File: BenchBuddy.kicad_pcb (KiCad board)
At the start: 4 copper layers, 165.1 x 63.5 mm, 56 parts, among them K1 1461069-5, P1 24 pin MiniFit JR, P2 CONN_3X2, P3 CONN_2, P4 12 pin Terminal Block, P5 3 Pin TB, Q1 2N3904, U1 MCP3901, U2 OPA4170, U3 LMT84, U9 LTV-816S

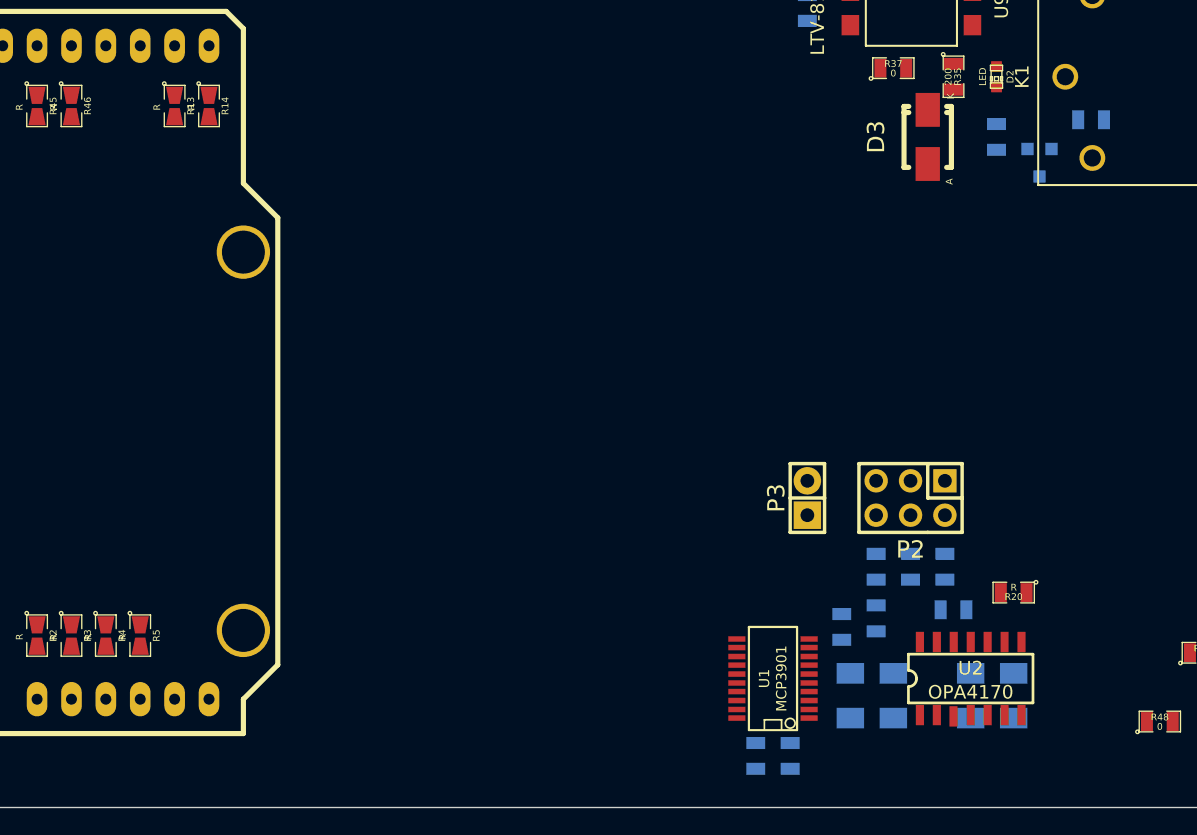
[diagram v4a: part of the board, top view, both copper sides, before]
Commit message: Associating and Placing the Current/Fan Driver Module
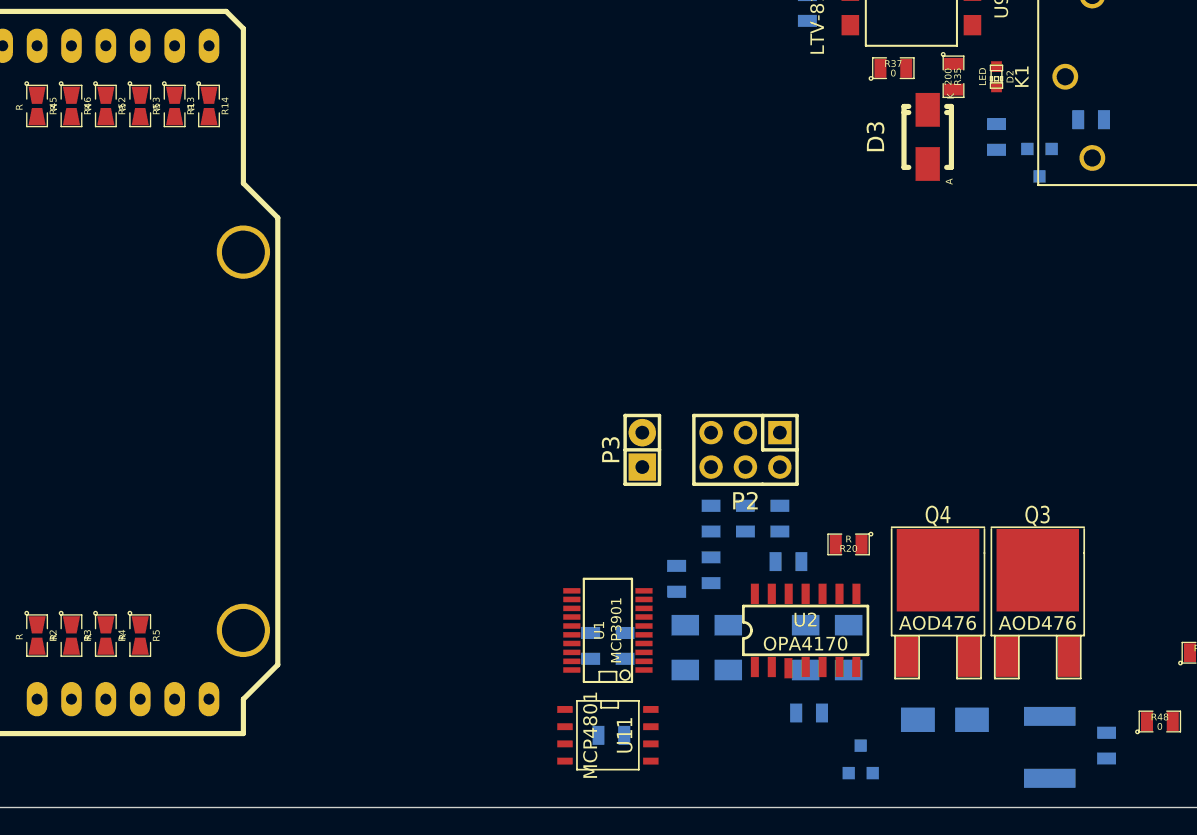
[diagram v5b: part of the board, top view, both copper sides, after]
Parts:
- added C10: C, SMD_Packages:SM0805, B.Cu at (165.9, 114.0)
- added C11: C, SMD_Packages:SM0805, B.Cu at (202.4, 114.8)
- added D5: B130-13-F, Diodes_SMD:Diode-SMA_Standard, B.Cu at (190.5, 112.9)
- added Q2: DMN65D8L-7, SMD_Packages:SOT23GDS, B.Cu at (184.3, 115.8)
- added Q3: AOD476, SMD_Packages:DPAKGDS, F.Cu at (197.4, 108.2)
- added Q4: AOD476, SMD_Packages:DPAKGDS, F.Cu at (190.0, 108.2)
- added R41: R, SMD_Packages:SM0805, B.Cu at (180.5, 112.4)
- added R42: R, SMD_Packages:SM1206, B.Cu at (193.5, 101.6)
- added R52: R, BenchBudEE:SM0805-Bridge, F.Cu at (128.5, 67.6)
- added R53: R, BenchBudEE:SM0805-Bridge, F.Cu at (131.1, 67.6)
- added TH5: PTC, SMD_Packages:SM1812, B.Cu at (198.2, 114.9)
- added U11: MCP4801, SMD_Packages:SO8N, F.Cu at (165.6, 114.0)
- moved C6 14.7 mm to (164.3, 107.4)
- moved C7 14.7 mm to (166.9, 107.4)
- moved C1 12.7 mm to (170.7, 102.5)
- moved P2 12.7 mm to (175.8, 93.0)
- moved P3 12.7 mm to (168.1, 93.0)
- moved R17 12.7 mm to (174.5, 107.6)
- moved R18 12.7 mm to (183.4, 107.6)
- moved R19 12.7 mm to (180.2, 107.6)
- moved R20 12.7 mm to (183.4, 99.9)
- moved R21 12.7 mm to (178.3, 98.0)
- moved R44 12.7 mm to (175.8, 98.0)
- moved U1 12.7 mm to (165.6, 106.3)
- moved U2 12.7 mm to (180.2, 106.3)
- moved C8 12.7 mm to (178.9, 101.2)
- moved R16 12.7 mm to (171.3, 107.6)
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
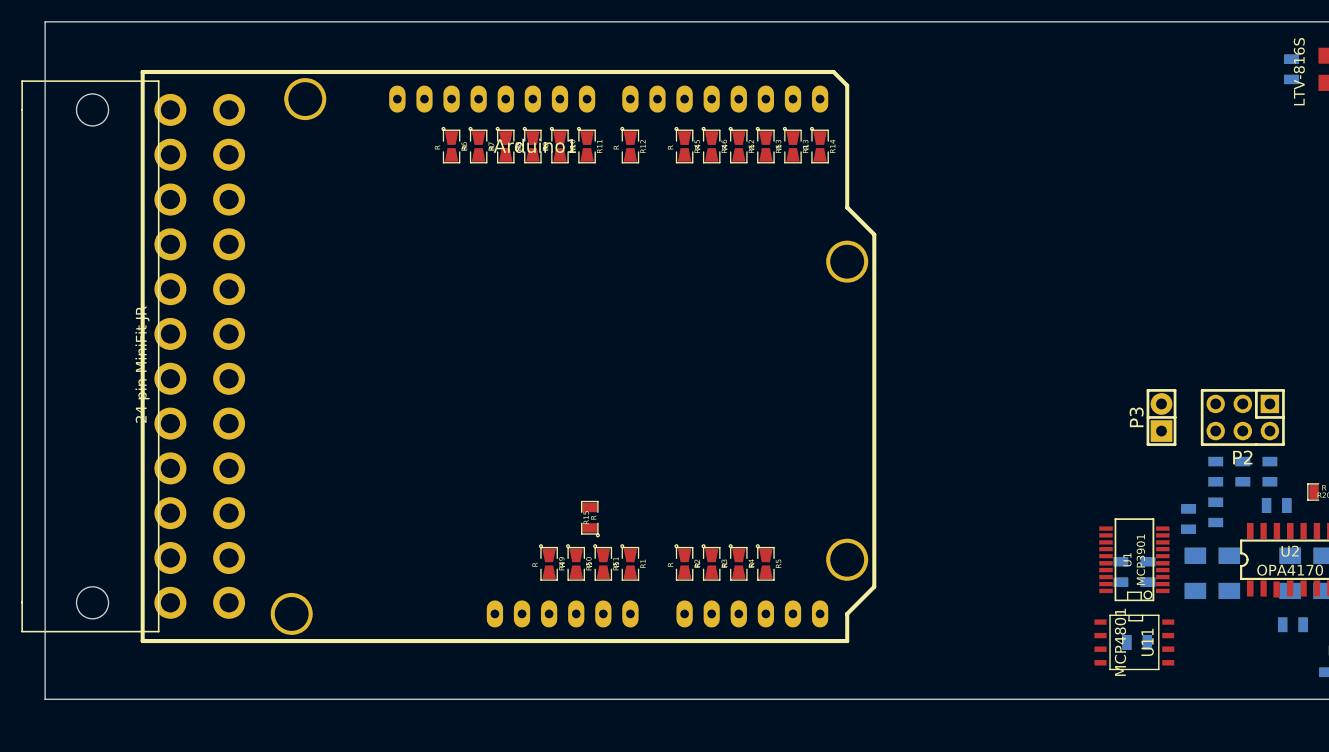
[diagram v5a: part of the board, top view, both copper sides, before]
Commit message: Associating and Placing the Power Protection and Filtering Module
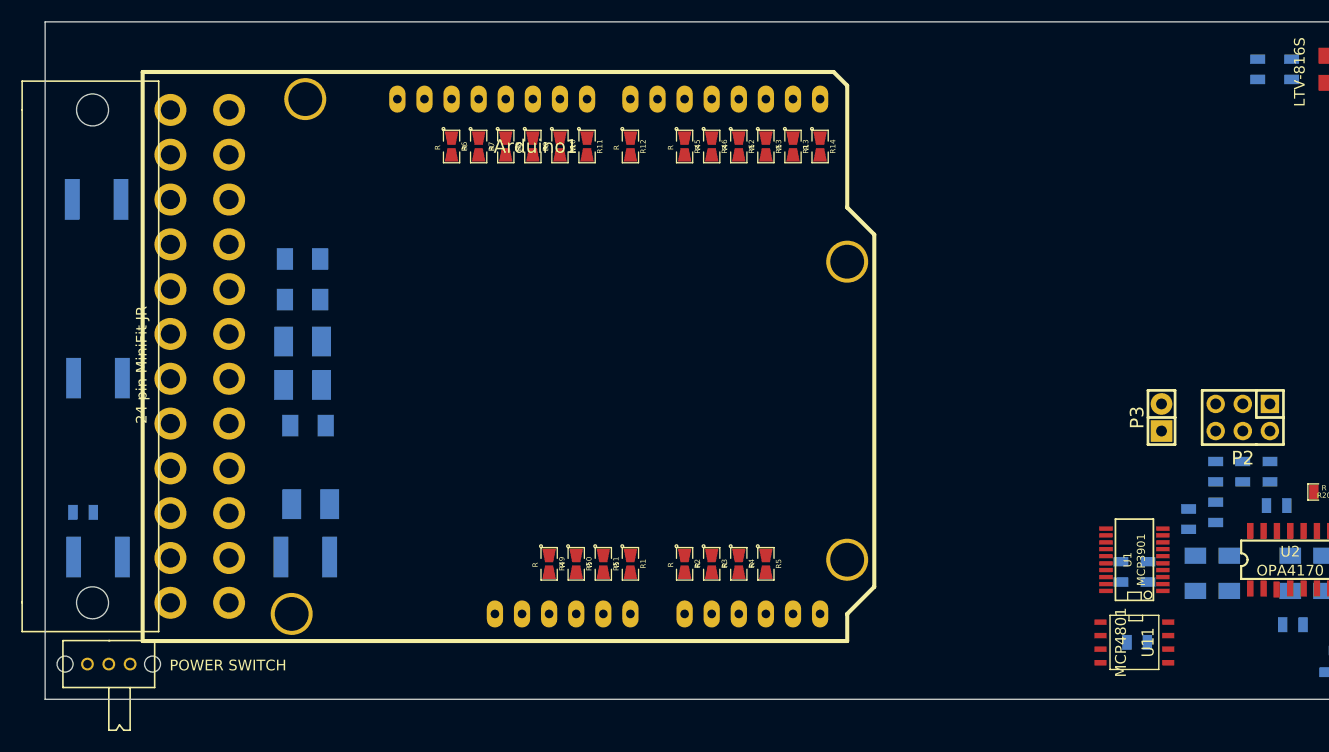
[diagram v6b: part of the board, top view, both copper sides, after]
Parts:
- added C12: C, SMD_Packages:SM1206, B.Cu at (87.6, 78.1)
- added C2: C, SMD_Packages:SM1206, B.Cu at (87.6, 81.9)
- added C3: C, SMD_Packages:SM1206, B.Cu at (88.1, 93.7)
- added L1: 22uH, SMD_Packages:SM1210L, B.Cu at (87.6, 89.9)
- added L2: 22uH, SMD_Packages:SM1210L, B.Cu at (88.4, 101.1)
- added L4: 22uH, SMD_Packages:SM1210L, B.Cu at (87.6, 85.9)
- added R23: R, SMD_Packages:SM0805, B.Cu at (67.1, 101.9)
- added SW1: POWER SWITCH, BenchBudEE:SLIDE_SWITCH_SPDT, F.Cu at (69.5, 116.1)
- added TH1: PTC, SMD_Packages:SM1812, B.Cu at (68.5, 106.0)
- added TH2: PTC, SMD_Packages:SM1812, B.Cu at (68.5, 89.3)
- added TH3: PTC, SMD_Packages:SM1812, B.Cu at (68.3, 72.5)
- added TH4: PTC, SMD_Packages:SM1812, B.Cu at (87.9, 106.0)
- R15: moved to B.Cu
- moved R15 75.4 mm to (177.2, 60.3)

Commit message: Merge CE BenchBudEE commit 00937c39d96b9ebb1b0292c11cc231788ab24edd
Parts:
- removed Arduino1: ARDUINO_SHIELD, Arduino:ARDUINO_SHIELD
- added ARD1: ARDUINOPINS, Arduino:ARDUINO_SHIELD, F.Cu at (140.6, 154.1)
- added C13: C, Capacitors_SMD:c_0805, B.Cu at (270.1, 106.8)
- added C14: C, Capacitors_SMD:c_0805, B.Cu at (214.4, 109.4)
- added C15: C, Capacitors_SMD:c_0805, B.Cu at (235.6, 110.3)
- added C16: C, Capacitors_SMD:c_0805, B.Cu at (236.7, 147.1)
- added C17: C, Capacitors_SMD:c_0805, B.Cu at (217.5, 150.6)
- added C18: C, Capacitors_SMD:c_0805, B.Cu at (236.0, 141.3)
- added C19: C, Capacitors_SMD:c_0805, B.Cu at (213.7, 148.0)
- added C20: C, Capacitors_SMD:c_0805, B.Cu at (216.5, 116.1)
- added C21: C, Capacitors_SMD:c_0805, B.Cu at (233.9, 116.4)
- added C22: C, Capacitors_SMD:c_0805, B.Cu at (220.0, 147.3)
- added C23: C, Capacitors_SMD:c_0805, B.Cu at (238.6, 122.0)
- added C24: C, Capacitors_SMD:c_0805, B.Cu at (217.1, 110.5)
- added C25: C, Capacitors_SMD:c_0805, B.Cu at (236.3, 122.3)
- added C4: C, Capacitors_SMD:c_1206, F.Cu at (163.0, 144.4)
- added C5: 1U, Capacitors_SMD:c_0805, B.Cu at (276.9, 132.5)
- added D1: LG Q971-KN-1, LEDs:LED-0603, F.Cu at (260.3, 147.8)
- added D10: MMBD914-7-F, BenchBudEE:Diode_SOT23, F.Cu at (216.7, 119.6)
- added D11: MMBD914-7-F, BenchBudEE:Diode_SOT23, F.Cu at (238.0, 142.6)
- added D12: MMBD914-7-F, BenchBudEE:Diode_SOT23, F.Cu at (241.5, 120.0)
- added D4: B130-13-F, Diodes_SMD:Diode-SMA_Standard, F.Cu at (279.1, 114.4)
- added D6: MMBD914-7-F, BenchBudEE:Diode_SOT23, F.Cu at (211.9, 140.9)
- added D7: MMBD914-7-F, BenchBudEE:Diode_SOT23, F.Cu at (239.4, 115.9)
- added D8: MMBD914-7-F, BenchBudEE:Diode_SOT23, F.Cu at (213.1, 147.7)
- added D9: MMBD914-7-F, BenchBudEE:Diode_SOT23, F.Cu at (216.1, 122.5)
- added L3: CM322522-220KL, SMD_Packages:SM1210L, F.Cu at (162.2, 140.4)
- added R24: R, Resistors_SMD:Resistor_SMD0805_HandSoldering, B.Cu at (233.8, 122.2)
- added R25: R, Resistors_SMD:Resistor_SMD0805_HandSoldering, B.Cu at (233.8, 148.2)
- added R26: R, BenchBudEE:SM0805-Bridge, F.Cu at (178.4, 146.9)
- added R27: R, BenchBudEE:SM0805-Bridge, F.Cu at (181.0, 146.9)
- added R28: R, BenchBudEE:SM0805-Bridge, F.Cu at (183.4, 146.9)
- added R29: R, BenchBudEE:SM0805-Bridge, F.Cu at (186.3, 146.7)
- added R30: R, BenchBudEE:SM0805-Bridge, F.Cu at (190.1, 147.3)
- added R31: R, BenchBudEE:SM0805-Bridge, F.Cu at (193.0, 147.4)
- added R32: R, BenchBudEE:SM0805-Bridge, F.Cu at (195.5, 147.6)
- added R33: R, BenchBudEE:SM0805-Bridge, F.Cu at (198.4, 147.3)
- added R40: R, BenchBudEE:SM0805-Bridge, F.Cu at (185.9, 107.3)
- added R54: R, Resistors_SMD:Resistor_SMD0805_HandSoldering, B.Cu at (215.0, 114.2)
- added R55: R, Resistors_SMD:Resistor_SMD0805_HandSoldering, B.Cu at (211.6, 113.2)
- added U4: OPA4170, SOIC_Packages:SOIC-14_Narrow, F.Cu at (269.0, 116.1)
- added U5: MCP4801, SMD_Packages:SO8N, F.Cu at (253.8, 120.0)
- added U6: LM337T, Transistors_TO-220:TO-220_Neutral123_Horizontal, F.Cu at (235.8, 145.8)
- added U7: AP5726, Housings_SOT-23_SOT-143_TSOT-6:TSOT6-MK06A-Housing, F.Cu at (279.2, 132.6)
- added U8: LM337T, Transistors_TO-220:TO-220_Neutral123_Horizontal, F.Cu at (235.8, 102.3)
- added V2006B: VAL**, V2006B, F.Cu at (244.9, 105.7)
- added V2006B: VAL**, V2006B, F.Cu at (224.6, 106.2)
- C1, C10, C7, C8, C9: footprint SMD_Packages:SM0805 -> Capacitors_SMD:c_0805
- C11: footprint SMD_Packages:SM0805 -> Capacitors_SMD:c_0805; moved to F.Cu
- C12: footprint SMD_Packages:SM1206 -> Capacitors_SMD:c_0805
- C2: footprint SMD_Packages:SM1206 -> Capacitors_SMD:c_1206
- C3: footprint SMD_Packages:SM1206 -> Capacitors_SMD:c_1206; moved to F.Cu
- C6: value C -> 1U; footprint SMD_Packages:SM0805 -> Capacitors_SMD:c_0805
- D2: value LED -> B130-13-F; footprint LEDs:LED-0603 -> Diodes_SMD:Diode-SMA_Standard
- D3: value B130-13-F -> MMBD914-7-F; footprint Diodes_SMD:Diode-SMA_Standard -> BenchBudEE:Diode_SOT23
- D5: value B130-13-F -> B0540WS-7; footprint Diodes_SMD:Diode-SMA_Standard -> BenchBudEE:DIODE_SOD-323; moved to F.Cu
- L1: value 22uH -> CM322522-220KL
- L2: value 22uH -> CM322522-220KL; moved to F.Cu
- L4: value 22uH -> 22u; footprint SMD_Packages:SM1210L -> BenchBudEE:INDUCTOR_NR4012T220M; moved to F.Cu
- P1: value 24 pin MiniFit JR -> 24 Pin MiniFit JR
- P4: value 12 pin Terminal Block -> 12 Pin Terminal Block
- Q2: moved to F.Cu
- Q3, Q4: footprint SMD_Packages:DPAKGDS -> SMD_Packages:DPAK2
- R1: value R -> 500; footprint BenchBudEE:SM0805-Bridge -> Resistors_SMD:Resistor_SMD0805_HandSoldering; moved to B.Cu
- R10, R7, R8, R9: footprint BenchBudEE:SM0805-Bridge -> Resistors_SMD:Resistor_SMD1206_HandSoldering; moved to B.Cu
- R11, R14: footprint BenchBudEE:SM0805-Bridge -> Resistors_SMD:Resistor_SMD0805_HandSoldering
- R12, R13, R45, R52, R53: footprint BenchBudEE:SM0805-Bridge -> Resistors_SMD:Resistor_SMD0805_HandSoldering; moved to B.Cu
- R15, R22, R23, R43, R44, R48: footprint SMD_Packages:SM0805 -> Resistors_SMD:Resistor_SMD0805_HandSoldering
- R16: footprint SMD_Packages:SM1206 -> Resistors_SMD:Resistor_SMD1206_HandSoldering
- R17: value R -> 15; footprint SMD_Packages:SM1206 -> Resistors_SMD:Resistor_SMD0805_HandSoldering
- R18: value R -> 715; footprint SMD_Packages:SM1206 -> Resistors_SMD:Resistor_SMD0805_HandSoldering
- R19: value R -> 5K; footprint SMD_Packages:SM1206 -> BenchBudEE:POT-EVUE3K; moved to F.Cu
- R2: value R -> 200; footprint BenchBudEE:SM0805-Bridge -> Resistors_SMD:Resistor_SMD0805_HandSoldering; moved to B.Cu
- R20: value R -> 5K; footprint SMD_Packages:SM0805 -> BenchBudEE:POT-EVUE3K
- R21: value R -> 715; footprint SMD_Packages:SM0805 -> Resistors_SMD:Resistor_SMD0805_HandSoldering
- R3, R49: value R -> 0; footprint BenchBudEE:SM0805-Bridge -> Resistors_SMD:Resistor_SMD0805_HandSoldering
- R34: value 500 -> R; footprint SMD_Packages:SM0805 -> BenchBudEE:SM0805-Bridge; moved to F.Cu
- R35: value 200 -> R; footprint SMD_Packages:SM0805 -> BenchBudEE:SM0805-Bridge
- R36: value 100 -> R; footprint SMD_Packages:SM0805 -> BenchBudEE:SM0805-Bridge; moved to F.Cu
- R37, R47: value 0 -> R; footprint SMD_Packages:SM0805 -> BenchBudEE:SM0805-Bridge
- R38, R39: value 0 -> R; footprint SMD_Packages:SM0805 -> BenchBudEE:SM0805-Bridge; moved to F.Cu
- R4: value R -> 100; footprint BenchBudEE:SM0805-Bridge -> Resistors_SMD:Resistor_SMD0805_HandSoldering; moved to B.Cu
- R41: footprint SMD_Packages:SM0805 -> BenchBudEE:SM0805-Bridge; moved to F.Cu
- R42: footprint SMD_Packages:SM1206 -> BenchBudEE:SM0805-Bridge; moved to F.Cu
- R5, R6: value R -> 0; footprint BenchBudEE:SM0805-Bridge -> Resistors_SMD:Resistor_SMD0805_HandSoldering; moved to B.Cu
- SW1: value POWER SWITCH -> Power Switch
- TH1, TH2, TH3, TH4: value PTC -> MINISMDC050F-2
- TH5: value PTC -> MINISMDC050F-2; moved to F.Cu
- U1: value MCP3901 -> LTV-816S; footprint SMD_Packages:SSOP20 -> BenchBudEE:SMD-4
- U11: value MCP4801 -> LM317; footprint SMD_Packages:SO8N -> Transistors_TO-220:TO-220_Neutral123_Horizontal
- U2: value OPA4170 -> MCP3901; footprint SOIC_Packages:SOIC-14_Narrow -> SMD_Packages:SSOP20
- U9: value LTV-816S -> LM317; footprint BenchBudEE:SMD-4 -> Transistors_TO-220:TO-220_Neutral123_Horizontal
- moved R6 193.8 mm to (273.5, 157.1), turned to 0 degrees
- moved L4 188.7 mm to (270.7, 131.3), turned to 270 degrees
- moved R49 180.1 mm to (290.2, 122.4), turned to 0 degrees
- moved C12 171.7 mm to (254.2, 119.8), turned to 90 degrees
- moved R7 165.4 mm to (261.7, 117.7)
- moved R10 164.4 mm to (268.3, 117.7), turned to 90 degrees
- moved R9 163.7 mm to (265.0, 117.7), turned to 90 degrees
- moved R8 160.9 mm to (258.9, 119.9)
- moved R11 157.4 mm to (266.5, 107.7), turned to 180 degrees
- moved R12 153.9 mm to (266.5, 109.2)
- moved R23 152.5 mm to (218.7, 118.1), turned to 270 degrees
- moved R45 146.6 mm to (264.0, 109.2)
- moved R1 142.9 mm to (256.7, 142.6)
- moved R5 142.7 mm to (269.8, 140.2), turned to 0 degrees
- moved R2 140.5 mm to (257.8, 147.8), turned to 90 degrees
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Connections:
- C10 pad 1: +5V -> AGND
- C10 pad 2: AGND -> FE_V-
- C11 pad 1: +12C -> +5V
- C12 pad 1: +12V -> AGND
- C12 pad 2: GND -> +5V
- C2 pad 1: +12V -> +5V
- C3 pad 1: GND -> +12V
- C3 pad 2: -12V -> GND
- C6 pad 1: AGND -> /LED_Driver/LED_STRING+
- C6 pad 2: +5V -> GND
- C7 pad 1: +5V -> AGND
- C7 pad 2: AGND -> +5V
- C8 pad 1: AGND -> +5V
- C8 pad 2: -12V -> AGND
- C9 pad 1: +5V -> AGND
- C9 pad 2: AGND -> FE_V+
- D2 pad 1: Net-(D2-Pad1) -> N-0000091
- D2 pad 2: Net-(D2-Pad2) -> N-0000090
- D3 pad 1: Net-(D3-Pad1) -> /PowerAdjustmentMonitor/V-_ADJ
- D3 pad 2: Net-(D3-Pad2) -> -12V
- D5 pad 1: /Fan/FAN_OUT- -> N-00000117
- D5 pad 2: /Fan/FAN_OUT+ -> /LED_Driver/LED_STRING+
- K1 pad 2: Net-(D3-Pad2) -> N-0000090
- K1 pad 3: /Relay/RELAY_NO -> /Relay/RELAY_NC
- K1 pad 4: /Relay/RELAY_NC -> /Relay/RELAY_NO
- K1 pad 5: Net-(D3-Pad1) -> N-0000091
- L1 pad 1: +12P -> +5P
- L1 pad 2: +12V -> +5V
- L4 pad 1: +12P -> +5P
- L4 pad 2: +12V -> N-00000117
- P1 pad 12: Net-(P1-Pad12) -> N-0000095
- P1 pad 2: Net-(P1-Pad2) -> N-0000095
- P2 pad 1: Net-(P2-Pad1) -> N-0000081
- P2 pad 2: Net-(P2-Pad2) -> N-0000072
- P2 pad 3: Net-(P2-Pad1) -> N-0000081
- P2 pad 4: Net-(P2-Pad4) -> N-0000073
- P2 pad 5: Net-(P2-Pad1) -> N-0000081
- P2 pad 6: Net-(P2-Pad6) -> N-0000074
- P3 pad 1: Net-(P3-Pad1) -> N-0000064
- P3 pad 2: Net-(P3-Pad2) -> N-0000063
- P4 pad 1: +3.3V -> /LED_Driver/LED_STRING+
- P4 pad 11: /Terminal_Block/TC_IN+ -> /Fan/FAN_OUT-
- P4 pad 12: /Terminal_Block/TC_IN- -> /Fan/FAN_OUT+
- P4 pad 2: +5V -> /LED_Driver/LED_STRING-
- P4 pad 4: /Power Adjustment Monitor/V+_ADJ -> /PowerAdjustmentMonitor/V+_ADJ
- P4 pad 5: /Power Adjustment Monitor/V-_ADJ -> /PowerAdjustmentMonitor/V-_ADJ
- P4 pad 6: /LED_Driver/LED_STRING+ -> +3.3V
- P4 pad 7: /LED_Driver/LED_STRING- -> +5V
- P4 pad 8: /Fan/FAN_OUT+ -> /Thermocouple/TC IN +
- P4 pad 9: /Fan/FAN_OUT- -> /Thermocouple/TC IN -
- Q1 pad 1: Net-(Q1-Pad1) -> N-0000089
- Q1 pad 2: Net-(Q1-Pad2) -> N-0000088
- Q1 pad 3: Net-(D3-Pad1) -> N-0000091
- Q2 pad D: Net-(Q2-PadD) -> N-00000119
- R1 pad 1: +12P -> /Arduino/RELAY-
- R1 pad 2: Net-(Arduino1-PadV_IN) -> N-0000085
- R10 pad 1: Net-(Arduino1-Pad9) -> N-0000083
- R10 pad 2: /Arduino/LED_EN_PWM -> N-0000077
- R11 pad 1: Net-(Arduino1-Pad8) -> N-0000076
- R11 pad 2: /Arduino/~ADC_CS -> N-0000081
- R12 pad 1: Net-(Arduino1-Pad7) -> N-0000072
- R12 pad 2: /Fan/~CS -> N-0000082
- R13 pad 1: Net-(Arduino1-Pad1) -> N-0000082
- R13 pad 2: /Arduino/RELAY+ -> N-0000077
- R14 pad 1: Net-(Arduino1-Pad0) -> N-0000096
- R14 pad 2: /Arduino/FAN_MODE -> +3.3V
- R15 pad 1: GND -> N-00000120
- R15 pad 2: /Arduino/RELAY- -> N-00000119
- R16 pad 1: /Thermocouple/CH0+ -> /Arduino/CURR_MEAS
- R16 pad 2: Net-(R16-Pad2) -> GND
- R17 pad 1: AGND -> /LED_Driver/LED_STRING-
- R17 pad 2: Net-(R17-Pad2) -> GND
- R18 pad 1: Net-(R16-Pad2) -> N-00000125
- R18 pad 2: Net-(R18-Pad2) -> /PowerAdjustmentMonitor/V-_ADJ
- R19 pad 1: Net-(R17-Pad2) -> N-00000125
- R19 pad 2: Net-(R19-Pad2) -> AGND
- R2 pad 1: /Arduino/V-_ADJ_MON -> N-0000084
- R2 pad 2: Net-(Arduino1-PadAD0) -> GND
- R20 pad 1: Net-(R18-Pad2) -> N-00000124
- R20 pad 2: Net-(P2-Pad1) -> AGND
- R21 pad 1: Net-(P2-Pad6) -> N-00000124
- R21 pad 2: Net-(R21-Pad2) -> /PowerAdjustmentMonitor/V+_ADJ
- R22 pad 1: Net-(R21-Pad2) -> /Arduino/V+_ADJ_MON
- R22 pad 2: Net-(R19-Pad2) -> /PowerAdjustmentMonitor/V+_ADJ
- R23 pad 1: Net-(R23-Pad1) -> AGND
- R23 pad 2: +3.3V -> /Arduino/V+_ADJ_MON
- R3 pad 1: /Arduino/V+_ADJ_MON -> +12P
- R3 pad 2: Net-(Arduino1-PadAD1) -> N-0000086
- R34 pad 1: /Arduino/RELAY- -> /Arduino/SCLK
- R34 pad 2: Net-(R34-Pad2) -> N-0000058
- R35 pad 1: GND -> /Arduino/MOSI
- R35 pad 2: Net-(D2-Pad2) -> N-0000059
- R36 pad 1: Net-(D2-Pad1) -> /Arduino/MISO
- R36 pad 2: Net-(Q1-Pad2) -> N-0000060
- R37 pad 1: Net-(R37-Pad1) -> /Arduino/FAN_PWM
- R37 pad 2: +12V -> N-0000054
- R38 pad 1: Net-(D3-Pad2) -> /Arduino/LED_EN_PWM
- R38 pad 2: +12V -> N-0000056
- R39 pad 1: GND -> /Arduino/~ADC_CS
- R39 pad 2: Net-(Q1-Pad1) -> N-0000049
- R4 pad 1: /Arduino/CURR_MEAS -> N-0000087
- R4 pad 2: Net-(Arduino1-PadAD2) -> N-0000088
- R41 pad 1: Net-(R41-Pad1) -> /Arduino/RELAY+
- R41 pad 2: Net-(Q2-PadD) -> N-0000055
- R42 pad 1: /Arduino/CURR_MEAS -> /Arduino/FAN_MODE
- R42 pad 2: AGND -> N-0000057
- R43 pad 1: Net-(P2-Pad4) -> /Arduino/RELAY-
- R43 pad 2: Net-(R21-Pad2) -> GND
- R44 pad 1: Net-(P2-Pad2) -> N-0000074
- R44 pad 2: Net-(R21-Pad2) -> N-0000082
- R45 pad 1: Net-(Arduino1-Pad5) -> N-0000073
- R45 pad 2: /Arduino/~RESET -> N-0000082
- R46 pad 1: Net-(Arduino1-Pad4) -> /Arduino/~RESET
- R46 pad 2: /Arduino/~DR -> N-0000041
- R47 pad 1: AGND -> /Arduino/~DR
- R47 pad 2: /Thermocouple/CH1- -> N-0000042
- R48 pad 2: /Thermocouple/CH0- -> /Thermocouple/CH1-
- R49 pad 1: +5V -> AGND
- R49 pad 2: Net-(Arduino1-Pad5V) -> /Thermocouple/CH0-
- R5 pad 1: /Fan/TACH_IN -> +12P
- R5 pad 2: Net-(Arduino1-PadAD3) -> N-0000090
- R50 pad 1: GND -> /Arduino/~LDAC
- R51 pad 1: GND -> /Arduino/~SHDN
- R52 pad 1: Net-(Arduino1-Pad3) -> AGND
- R52 pad 2: /Arduino/~LDAC -> N-00000122
- R53 pad 1: Net-(Arduino1-Pad2) -> N-00000122
- R53 pad 2: /Arduino/~SHDN -> FE_V-
- R6 pad 1: Net-(Arduino1-Pad13) -> N-0000089
- R6 pad 2: /Arduino/SCLK -> GND
- R7 pad 1: Net-(Arduino1-Pad12) -> AGND
- R7 pad 2: /Arduino/MISO -> N-0000083
- R8 pad 1: Net-(Arduino1-Pad11) -> /Thermocouple/CH0+
- R8 pad 2: /Arduino/MOSI -> N-0000075
- R9 pad 1: Net-(Arduino1-Pad10) -> N-0000075
- R9 pad 2: /Arduino/FAN_PWM -> N-0000076
- SW1 pad 1: Net-(R23-Pad1) -> N-0000096
- TH1 pad 1: Net-(P1-Pad2) -> N-0000095
- TH2 pad 2: +5V -> +5P
- U1 pad 1: /Arduino/~RESET -> /Arduino/RELAY+
- U1 pad 2: +5V -> N-0000085
- U1 pad 3: +5V -> N-0000087
- U1 pad 4: /Thermocouple/CH0+ -> N-0000086
- U11 pad 1: +5V -> +12V
- U11 pad 2: /Fan/~CS -> N-00000124
- U11 pad 3: /Arduino/SCLK -> /PowerAdjustmentMonitor/V+_ADJ
- U2 pad 1: /Thermocouple/CH0+ -> /Arduino/~RESET
- U2 pad 10: /Terminal_Block/TC_IN+ -> REF-
- U2 pad 11: -12V -> AGND
- U2 pad 12: /Terminal_Block/TC_IN- -> N-0000064
- U2 pad 13: Net-(R21-Pad2) -> N-0000063
- U2 pad 14: Net-(R19-Pad2) -> /Arduino/~DR
- U2 pad 2: Net-(R17-Pad2) -> +5V
- U2 pad 3: Net-(R16-Pad2) -> +5V
- U2 pad 4: +12V -> /Thermocouple/CH0+
- U2 pad 5: Net-(Q2-PadD) -> /Thermocouple/CH0-
- U2 pad 6: /Arduino/CURR_MEAS -> /Thermocouple/CH1-
- U2 pad 7: Net-(Q4-PadG) -> /Thermocouple/CH1+
- U2 pad 8: Net-(R18-Pad2) -> AGND
- U2 pad 9: Net-(P2-Pad1) -> REF+
- U9 pad 1: /Arduino/RELAY+ -> +12V
- U9 pad 2: Net-(R34-Pad2) -> N-00000123
- U9 pad 3: Net-(D2-Pad1) -> FE_V+
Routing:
- net +5P: track 0.00 -> 200.0 mm, vias 0 -> 1
- net +12C: track 0.00 -> 143.7 mm
- net +3.3V: track 0.00 -> 140.2 mm, vias 0 -> 1
- net N-0000095: track 0.00 -> 25.4 mm
- net +5V: track 0.00 -> 6.94 mm, vias 0 -> 1
- net GND: track 0.00 -> 6.63 mm, vias 0 -> 2
- net +12P: track 0.00 -> 2.99 mm, vias 0 -> 1
- net (no net): track 0.00 -> 0.86 mm
- added copper zone on PWR, net +12P
- added copper zone on PWR, net +12V
- added copper zone on PWR, net +3.3V
- added copper zone on PWR, net +5V
- added copper zone on PWR, net -12V
- added copper zone on GND, net AGND
- added copper zone on GND, net GND

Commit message: Layout Work Session 2
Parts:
- removed V2006B (x2): VAL**, V2006B
- added JP1: JUMPER, Pin_Headers:Pin_Header_Straight_2x01, F.Cu at (237.1, 61.0)
- added MH: MountingHole_3mm_RevA_Date21Jun2010, Mounting_Holes:MountingHole_3mm, F.Cu at (289.9, 98.6)
- added MH: MountingHole_3mm_RevA_Date21Jun2010, Mounting_Holes:MountingHole_3mm, F.Cu at (151.2, 156.5)
- added MH: MountingHole_3mm_RevA_Date21Jun2010, Mounting_Holes:MountingHole_3mm, F.Cu at (151.1, 98.4)
- ARD1: footprint Arduino:ARDUINO_SHIELD -> BenchBudEE:ARDUINO_SHIELD
- TH5: moved to B.Cu
- U11, U9: value LM317 -> LM317T; footprint Transistors_TO-220:TO-220_Neutral123_Horizontal -> Power_Integrations:TO-220
- U6, U8: footprint Transistors_TO-220:TO-220_Neutral123_Horizontal -> Power_Integrations:TO-220
- moved C20 119.3 mm to (319.3, 55.6)
- moved C23 119.3 mm to (341.4, 61.5)
- moved R53 119.3 mm to (340.8, 49.9)
- moved C15 119.3 mm to (338.4, 49.8)
- moved C21 119.3 mm to (336.8, 55.9)
- moved C24 119.3 mm to (319.9, 50.0)
- moved C25 119.3 mm to (339.1, 61.8)
- moved D10 119.3 mm to (319.5, 59.1)
- moved D7 119.3 mm to (342.2, 55.4)
- moved D9 119.3 mm to (318.9, 62.0)
- moved R24 119.3 mm to (336.6, 61.7)
- moved R54 119.3 mm to (317.8, 53.6)
- moved R55 119.3 mm to (314.5, 52.7)
- moved C14 119.3 mm to (317.2, 48.8)
- moved D12 119.3 mm to (344.3, 59.5)
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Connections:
- ARD1 pad 0: (no net) -> Net-(ARD1-Pad0)
- ARD1 pad 1: N-0000039 -> Net-(ARD1-Pad1)
- ARD1 pad 10: N-0000037 -> Net-(ARD1-Pad10)
- ARD1 pad 11: N-0000057 -> Net-(ARD1-Pad11)
- ARD1 pad 12: N-0000055 -> Net-(ARD1-Pad12)
- ARD1 pad 13: N-0000043 -> Net-(ARD1-Pad13)
- ARD1 pad 2: N-0000032 -> Net-(ARD1-Pad2)
- ARD1 pad 3: N-0000034 -> Net-(ARD1-Pad3)
- ARD1 pad 3V3: (no net) -> Net-(ARD1-Pad3V3)
- ARD1 pad 4: N-0000035 -> Net-(ARD1-Pad4)
- ARD1 pad 5: N-0000053 -> Net-(ARD1-Pad5)
- ARD1 pad 5V: (no net) -> Net-(ARD1-Pad5V)
- ARD1 pad 6: N-0000052 -> Net-(ARD1-Pad6)
- ARD1 pad 7: N-0000050 -> Net-(ARD1-Pad7)
- ARD1 pad 8: N-0000051 -> Net-(ARD1-Pad8)
- ARD1 pad 9: N-0000036 -> Net-(ARD1-Pad9)
- ARD1 pad AD0: (no net) -> Net-(ARD1-PadAD0)
- ARD1 pad AD1: (no net) -> Net-(ARD1-PadAD1)
- ARD1 pad AD2: (no net) -> Net-(ARD1-PadAD2)
- ARD1 pad AD3: (no net) -> Net-(ARD1-PadAD3)
- ARD1 pad AD4: (no net) -> Net-(ARD1-PadAD4)
- ARD1 pad AD5: (no net) -> Net-(ARD1-PadAD5)
- ARD1 pad AREF: (no net) -> Net-(ARD1-PadAREF)
- ARD1 pad GND1: (no net) -> Net-(ARD1-PadGND1)
- ARD1 pad GND2: (no net) -> Net-(ARD1-PadGND2)
- ARD1 pad GND3: (no net) -> Net-(ARD1-PadGND3)
- ARD1 pad RST: (no net) -> Net-(ARD1-PadRST)
- ARD1 pad V_IN: (no net) -> Net-(ARD1-PadV_IN)
- C19 pad 1: N-00000124 -> Net-(C19-Pad1)
- C20 pad 1: N-00000123 -> Net-(C20-Pad1)
- D10 pad 1: N-00000123 -> Net-(C20-Pad1)
- D8 pad 1: N-00000124 -> Net-(C19-Pad1)
- R20 pad 1: N-00000124 -> Net-(C19-Pad1)
- R21 pad 1: N-00000124 -> Net-(C19-Pad1)
- R26 pad 1: N-0000039 -> Net-(ARD1-PadRST)
- R27 pad 1: N-0000032 -> Net-(ARD1-PadGND1)
- R28 pad 1: N-0000034 -> Net-(ARD1-PadGND2)
- R29 pad 1: N-0000035 -> Net-(ARD1-PadV_IN)
- R30 pad 1: N-0000053 -> Net-(ARD1-PadAD0)
- R31 pad 1: N-0000052 -> Net-(ARD1-PadAD1)
- R32 pad 1: N-0000050 -> Net-(ARD1-PadAD2)
- R33 pad 1: N-0000051 -> Net-(ARD1-PadAD3)
- R34 pad 2: N-0000058 -> Net-(ARD1-Pad13)
- R35 pad 2: N-0000059 -> Net-(ARD1-Pad12)
- R36 pad 2: N-0000060 -> Net-(ARD1-Pad11)
- R37 pad 2: N-0000054 -> Net-(ARD1-Pad10)
- R38 pad 2: N-0000056 -> Net-(ARD1-Pad9)
- R39 pad 2: N-0000049 -> Net-(ARD1-Pad8)
- R40 pad 2: N-0000061 -> Net-(ARD1-Pad7)
- R41 pad 2: N-0000055 -> Net-(ARD1-Pad1)
- R42 pad 2: N-0000057 -> Net-(ARD1-Pad0)
- R46 pad 2: N-0000041 -> Net-(ARD1-Pad5)
- R47 pad 2: N-0000042 -> Net-(ARD1-Pad4)
- R50 pad 2: N-0000040 -> Net-(ARD1-Pad3)
- R51 pad 2: N-0000043 -> Net-(ARD1-Pad2)
- R54 pad 1: N-00000123 -> Net-(C20-Pad1)
- R55 pad 2: N-00000123 -> Net-(C20-Pad1)
- U11 pad 1: +12V -> Net-(C19-Pad1)
- U11 pad 2: N-00000124 -> /PowerAdjustmentMonitor/V+_ADJ
- U11 pad 3: /PowerAdjustmentMonitor/V+_ADJ -> +12V
- U9 pad 1: +12V -> Net-(C20-Pad1)
- U9 pad 2: N-00000123 -> FE_V+
- U9 pad 3: FE_V+ -> +12V
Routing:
- net +5P: track 200.0 -> 0.00 mm, vias 1 -> 0
- net +12C: track 143.7 -> 0.00 mm
- net +3.3V: track 140.2 -> 0.00 mm, vias 1 -> 0
- net Net-(P1-Pad12): track 25.4 -> 0.00 mm
- net +5V: track 6.94 -> 0.00 mm, vias 1 -> 0
- net GND: track 6.63 -> 0.00 mm, vias 2 -> 0
- net +12P: track 2.99 -> 0.00 mm, vias 1 -> 0
- net (no net): track 0.86 -> 0.00 mm
- removed copper zone on PWR, net +12P
- removed copper zone on PWR, net +12V
- removed copper zone on PWR, net +5V
- removed copper zone on PWR, net -12V
- removed copper zone on GND, net AGND
- removed copper zone on GND, net GND
